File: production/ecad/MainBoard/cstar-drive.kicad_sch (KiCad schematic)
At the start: 28 parts, among them J1 B4B-PH-K-S, J2 B4B-PH-K-S, U1 DRV8842PWPR, U2 DRV8842PWPR, X1 B2P-VH, X2 B2P-VH

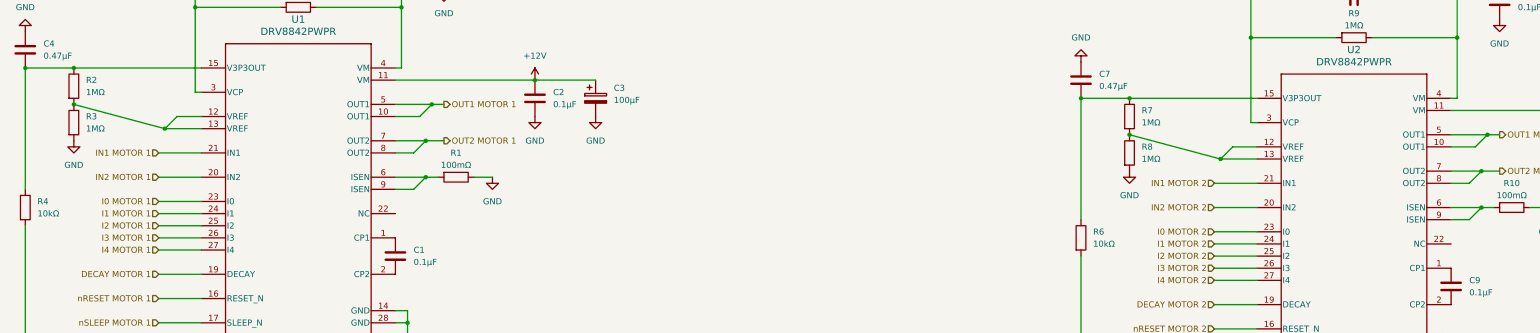
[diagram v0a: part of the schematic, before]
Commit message: "Updated Voltage Divider"
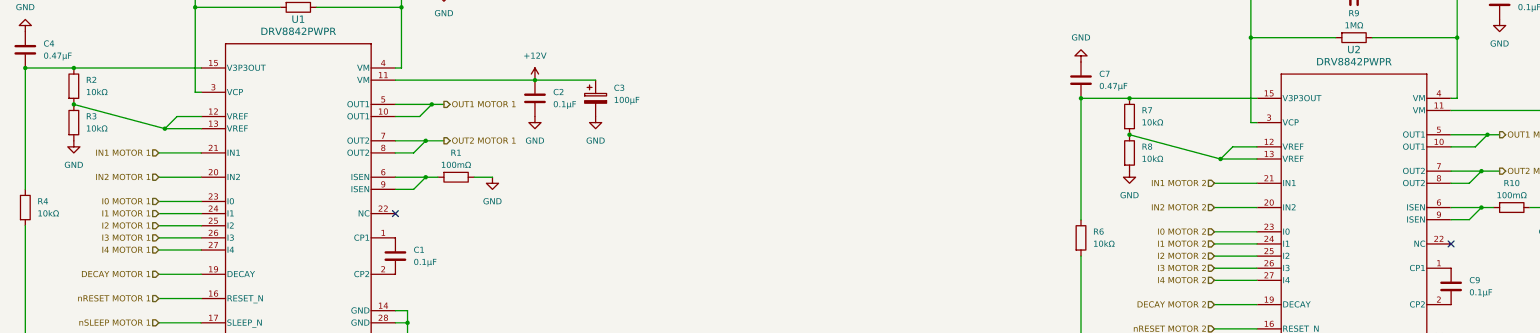
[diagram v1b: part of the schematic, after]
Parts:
- R2, R3, R7, R8: value 1MΩ -> 10kΩ
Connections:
- no-connect marks 0 -> 2
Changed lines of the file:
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@@
   (junction (at 349.25 110.49) (diameter 0) (color 0 0 0 0)
   )
+  (no_connect (at 121.92 111.76))
+  (no_connect (at 342.9 118.11))
   (wire (pts (xy 121.92 106.68) (xy 125.73 106.68))
     (stroke (width 0) (type default))
@@
       (effects (font (size 1.27 1.27)) (justify left))
     )
-    (property "Value" "1MΩ" (at 57.15 86.36 0)
+    (property "Value" "10kΩ" (at 57.15 86.36 0)
       (effects (font (size 1.27 1.27)) (justify left))
     )
@@
       (effects (font (size 1.27 1.27)) (justify left))
     )
-    (property "Value" "1MΩ" (at 278.13 100.33 0)
+    (property "Value" "10kΩ" (at 278.13 100.33 0)
       (effects (font (size 1.27 1.27)) (justify left))
     )
@@
       (effects (font (size 1.27 1.27)) (justify left))
     )
-    (property "Value" "1MΩ" (at 278.13 92.71 0)
+    (property "Value" "10kΩ" (at 278.13 92.71 0)
       (effects (font (size 1.27 1.27)) (justify left))
     )
@@
       (effects (font (size 1.27 1.27)) (justify left))
     )
-    (property "Value" "1MΩ" (at 57.15 93.98 0)
-      (effects (font (size 1.27 1.27)) (justify left))
-    )
+    (property "Value" "10kΩ" (at 57.15 93.98 0)
+      (effects (font (size 1.27 1.27)) (justify left))
+    )

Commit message: "Added Flyback Diode"
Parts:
- added U3: STPS10L25G-TR, D2PAK_STM, symbol STPS10L25G-TR:STPS10L25G-TR
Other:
- note added: "MOTOR 1 DRIVER"
- note added: "MOTOR 2 DRIVER"
- moved on the sheet: C1, C10, C11, C12, C2, C3, C4, C5, C6, C7, C8, C9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

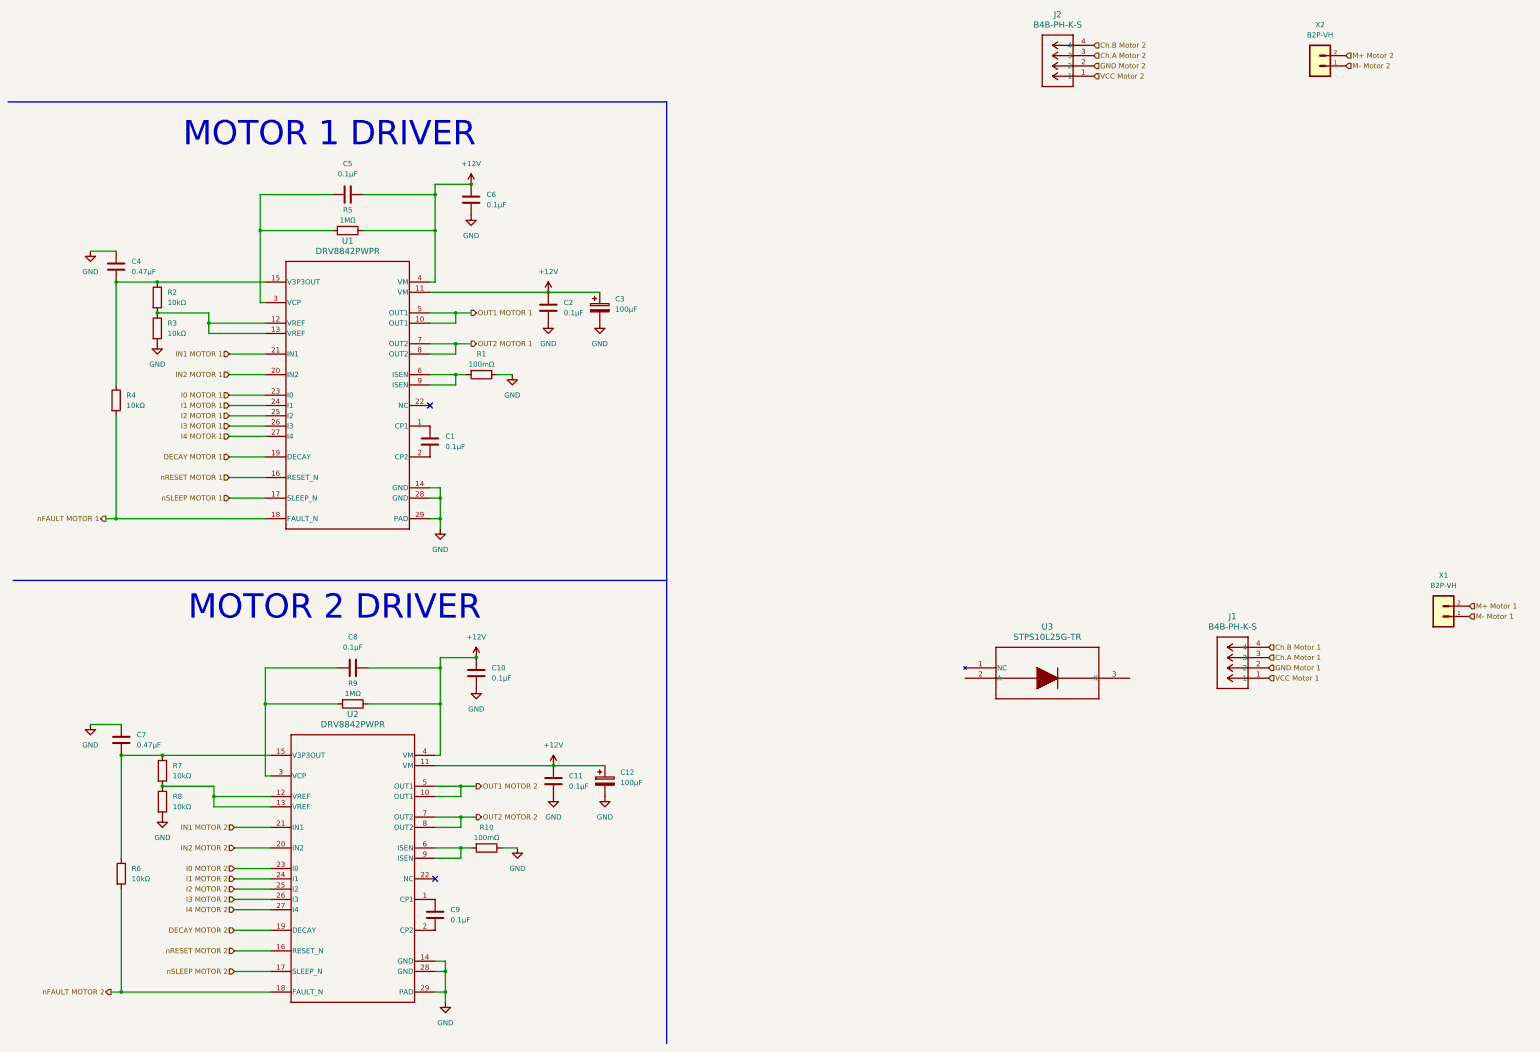
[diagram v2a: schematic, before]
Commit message: "Motor Controller IC Schematic v2"
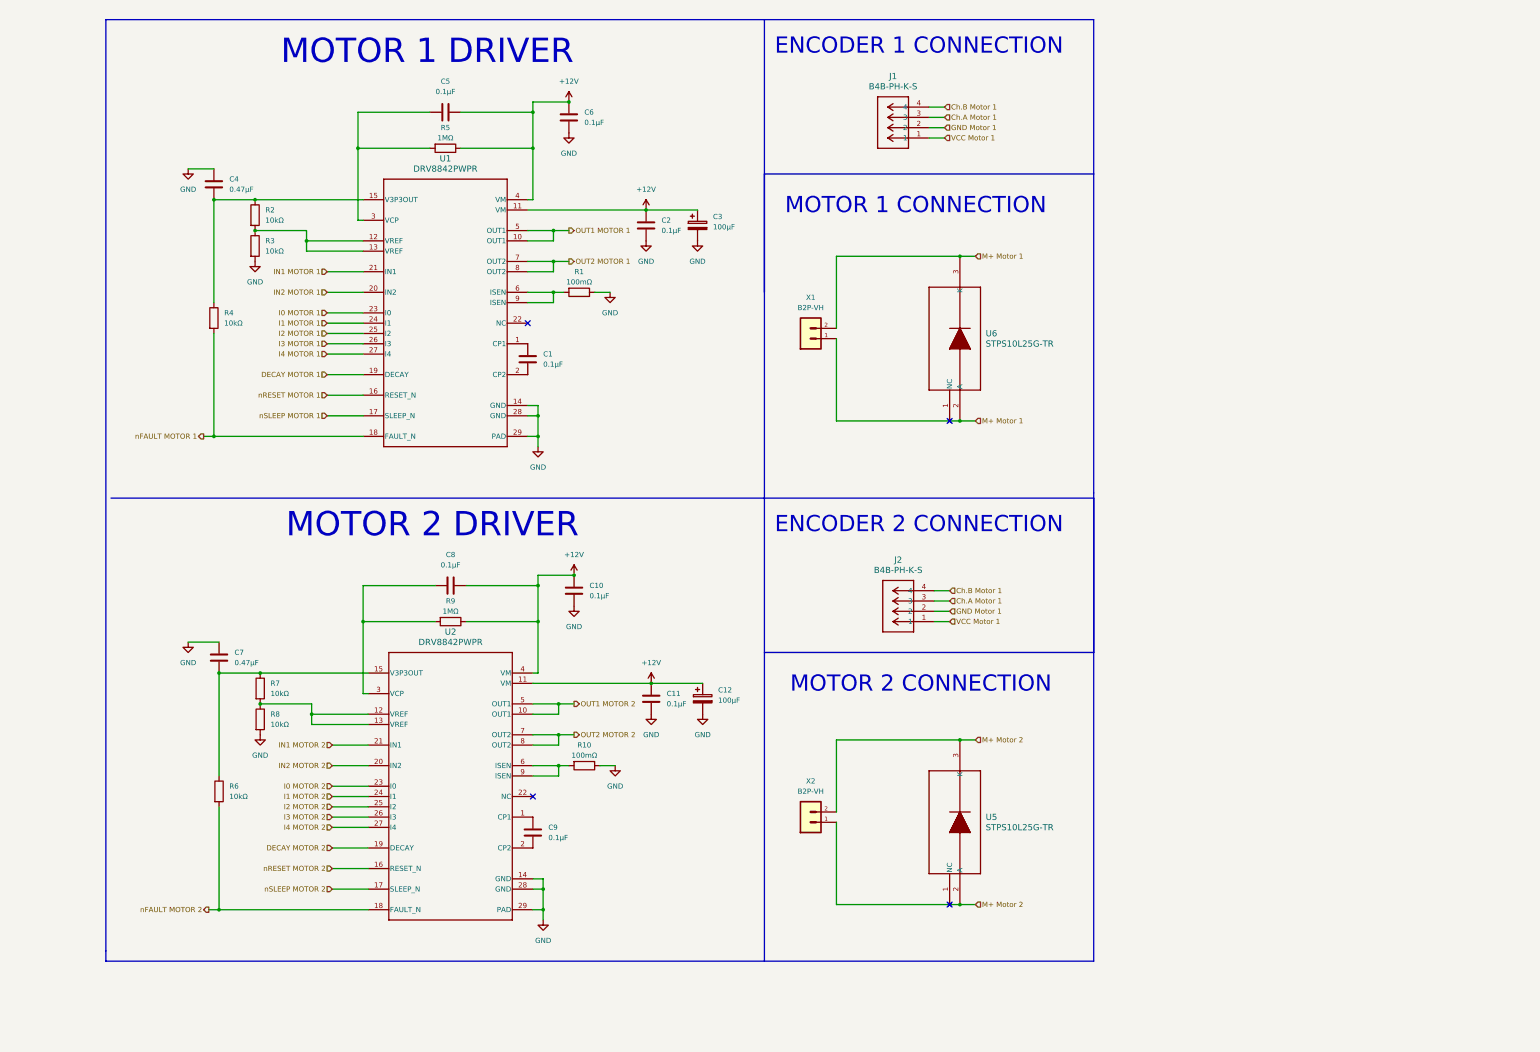
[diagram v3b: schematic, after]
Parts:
- removed U3: STPS10L25G-TR, D2PAK_STM, symbol STPS10L25G-TR:STPS10L25G-TR
- added U5, U6: STPS10L25G-TR, D2PAK_STM, symbol STPS10L25G-TR:STPS10L25G-TR
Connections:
- net Ch.A Motor 2 is gone; now on net Ch.A Motor 1: J2.3
- net Ch.B Motor 2 is gone; now on net Ch.B Motor 1: J2.4
- net GND Motor 2 is gone; now on net GND Motor 1: J2.2
- net M- Motor 1 is gone; now on net M+ Motor 1: X1.1
- net M- Motor 2 is gone; now on net M+ Motor 2: X2.1
- net VCC Motor 2 is gone; now on net VCC Motor 1: J2.1
- net M+ Motor 1: now also U6.2 (A), U6.3 (K)
- net M+ Motor 2: now also U5.2 (A), U5.3 (K)
- no-connect marks 2 -> 4
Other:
- note added: "ENCODER 1 CONNECTION"
- note added: "ENCODER 2 CONNECTION"
- note added: "MOTOR 1 CONNECTION"
- note added: "MOTOR 2 CONNECTION"
- moved on the sheet: C1, C10, C11, C12, C2, C3, C4, C5, C6, C7, C8, C9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

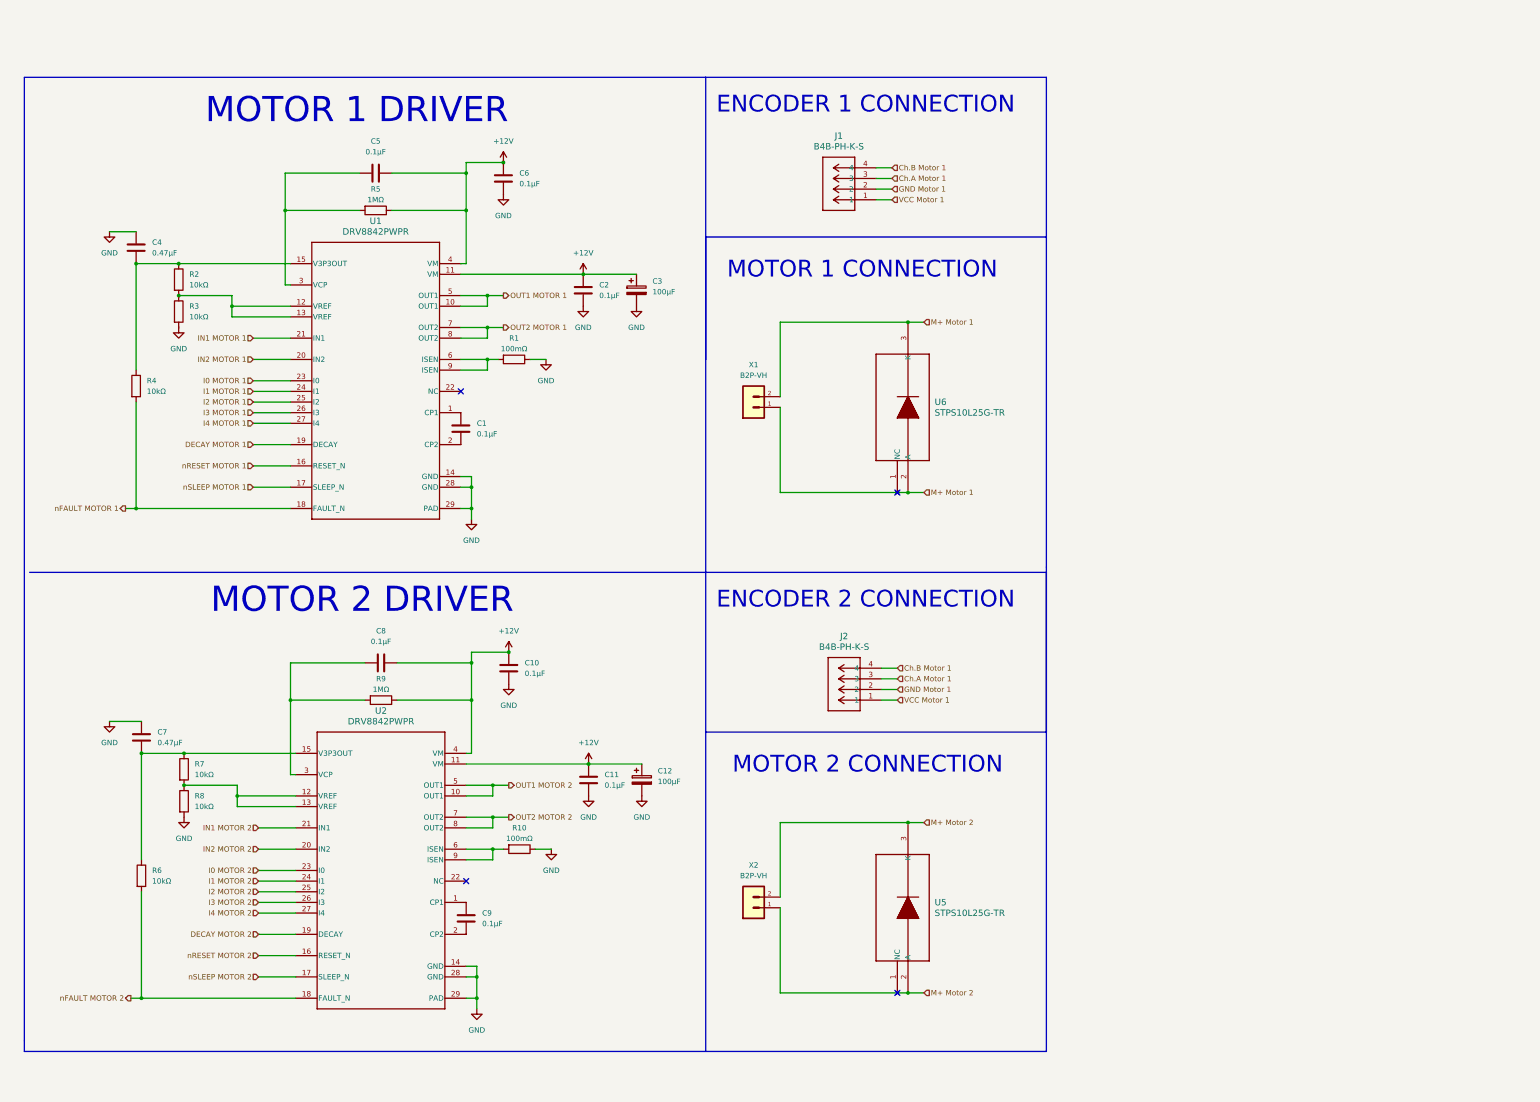
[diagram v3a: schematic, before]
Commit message: Added Test Points
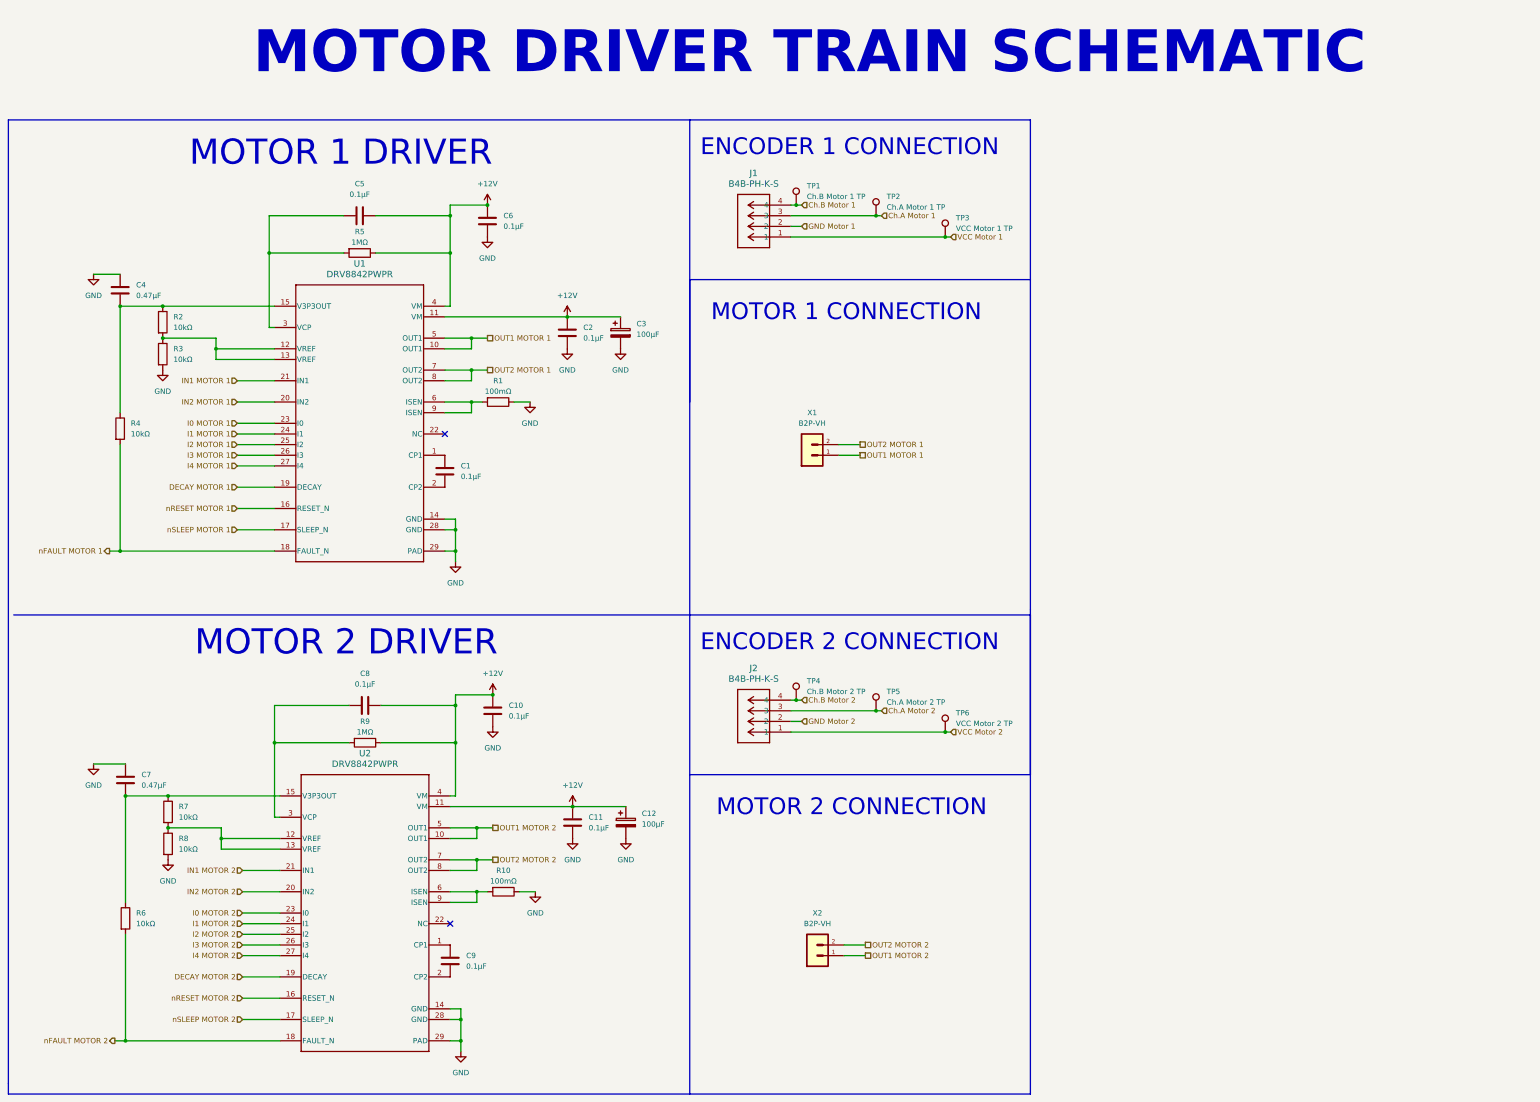
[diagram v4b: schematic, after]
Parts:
- removed U5, U6: STPS10L25G-TR, D2PAK_STM, symbol STPS10L25G-TR:STPS10L25G-TR
- added TP1: Ch.B Motor 1 TP, symbol Connector:TestPoint
- added TP2: Ch.A Motor 1 TP, symbol Connector:TestPoint
- added TP3: VCC Motor 1 TP, symbol Connector:TestPoint
- added TP4: Ch.B Motor 2 TP, symbol Connector:TestPoint
- added TP5: Ch.A Motor 2 TP, symbol Connector:TestPoint
- added TP6: VCC Motor 2 TP, symbol Connector:TestPoint
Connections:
- net Ch.A Motor 1: now also TP2.1; no longer J2.3
- net Ch.B Motor 1: now also TP1.1; no longer J2.4
- net GND Motor 1: no longer J2.2
- net OUT1 MOTOR 1: now also X1.1
- net OUT1 MOTOR 2: now also X2.1
- net OUT2 MOTOR 1: now also X1.2
- net OUT2 MOTOR 2: now also X2.2
- net VCC Motor 1: now also TP3.1; no longer J2.1
- removed net M+ Motor 1: X1.1, X1.2
- removed net M+ Motor 2: X2.1, X2.2
- new net Ch.A Motor 2: J2.3, TP5.1
- new net Ch.B Motor 2: J2.4, TP4.1
- new net GND Motor 2: J2.2
- new net VCC Motor 2: J2.1, TP6.1
- no-connect marks 4 -> 2
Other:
- note added: "MOTOR DRIVER TRAIN SCHEMATIC"
- moved on the sheet: C1, C10, C11, C12, C2, C3, C4, C5, C6, C7, C8, C9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

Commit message: "Motor Controller IC Schematic v3"
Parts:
- added TP10, TP5: ~, symbol Connector:TestPoint
- added TP11, TP12, TP13, TP14, TP15, TP16, TP17, TP18, TP19, TP20, TP21, TP22, TP23, TP24, TP25, TP26, TP27, TP28, TP29, TP30, TP31, TP32: IN1 MOTOR 1 TP, symbol Connector:TestPoint
- added TP4, TP9: OUT2 MOTOR 1 TP, symbol Connector:TestPoint
- added U3, U4: STPS10L25G-TR, D2PAK_STM, symbol STPS10L25G-TR:STPS10L25G-TR
- TP1: value Ch.B Motor 1 TP -> TestPoint
- TP2: value Ch.A Motor 1 TP -> TestPoint
- TP3: value VCC Motor 1 TP -> TestPoint
- renumbered TP4 to TP6, TP5 to TP7, TP6 to TP8
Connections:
- net DECAY MOTOR 2 is gone; now on net DECAY MOTOR 1: U2.19 (DECAY)
- net OUT1 MOTOR 1 is gone; now on net GND: U1.10 (OUT1), U1.5 (OUT1), X1.1
- net OUT1 MOTOR 2 is gone; now on net GND: U2.10 (OUT1), U2.5 (OUT1), X2.1
- net OUT2 MOTOR 1 is gone; now on net +12V: U1.7 (OUT2), U1.8 (OUT2), X1.2
- net OUT2 MOTOR 2 is gone; now on net +12V: U2.7 (OUT2), U2.8 (OUT2), X2.2
- net nRESET MOTOR 2 is gone; now on net nRESET MOTOR 1: U2.16 (RESET_N)
- net nSLEEP MOTOR 2 is gone; now on net nSLEEP MOTOR 1: U2.17 (SLEEP_N)
- net +12V: now also TP21.1, TP32.1, TP4.1, TP9.1, U3.3 (K), U4.3 (K)
- net DECAY MOTOR 1: now also TP18.1, TP27.1
- net GND: now also TP10.1, TP20.1, TP31.1, TP5.1, U3.2 (A), U4.2 (A)
- net I0 MOTOR 1: now also TP13.1
- net I0 MOTOR 2: now also TP30.1
- net I1 MOTOR 1: now also TP14.1
- net I1 MOTOR 2: now also TP26.1
- net I2 MOTOR 1: now also TP15.1
- net I2 MOTOR 2: now also TP25.1
- net I3 MOTOR 1: now also TP16.1
- net I3 MOTOR 2: now also TP24.1
- net I4 MOTOR 1: now also TP17.1
- net I4 MOTOR 2: now also TP23.1
- net IN1 MOTOR 1: now also TP11.1
- net IN1 MOTOR 2: now also TP28.1
- net IN2 MOTOR 1: now also TP12.1
- net IN2 MOTOR 2: now also TP29.1
- net nFAULT MOTOR 1: now also TP19.1
- net nFAULT MOTOR 2: now also TP22.1
- no-connect marks 2 -> 4
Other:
- moved on the sheet: C1, C2, C3, C4, C5, C6, J1, J2, R1, R2, R3, R4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
